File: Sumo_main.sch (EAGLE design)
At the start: 32 parts, among them U1 ATMEGA8U2AU, U2 SN65HVD3082ED, X1 MINI-USB-SCHIELD-32005-201, X2 RS485, X4 IR Sensor 1, X5 IR Sensor 2, X6 IR Sensor 3, Y1 16MHz

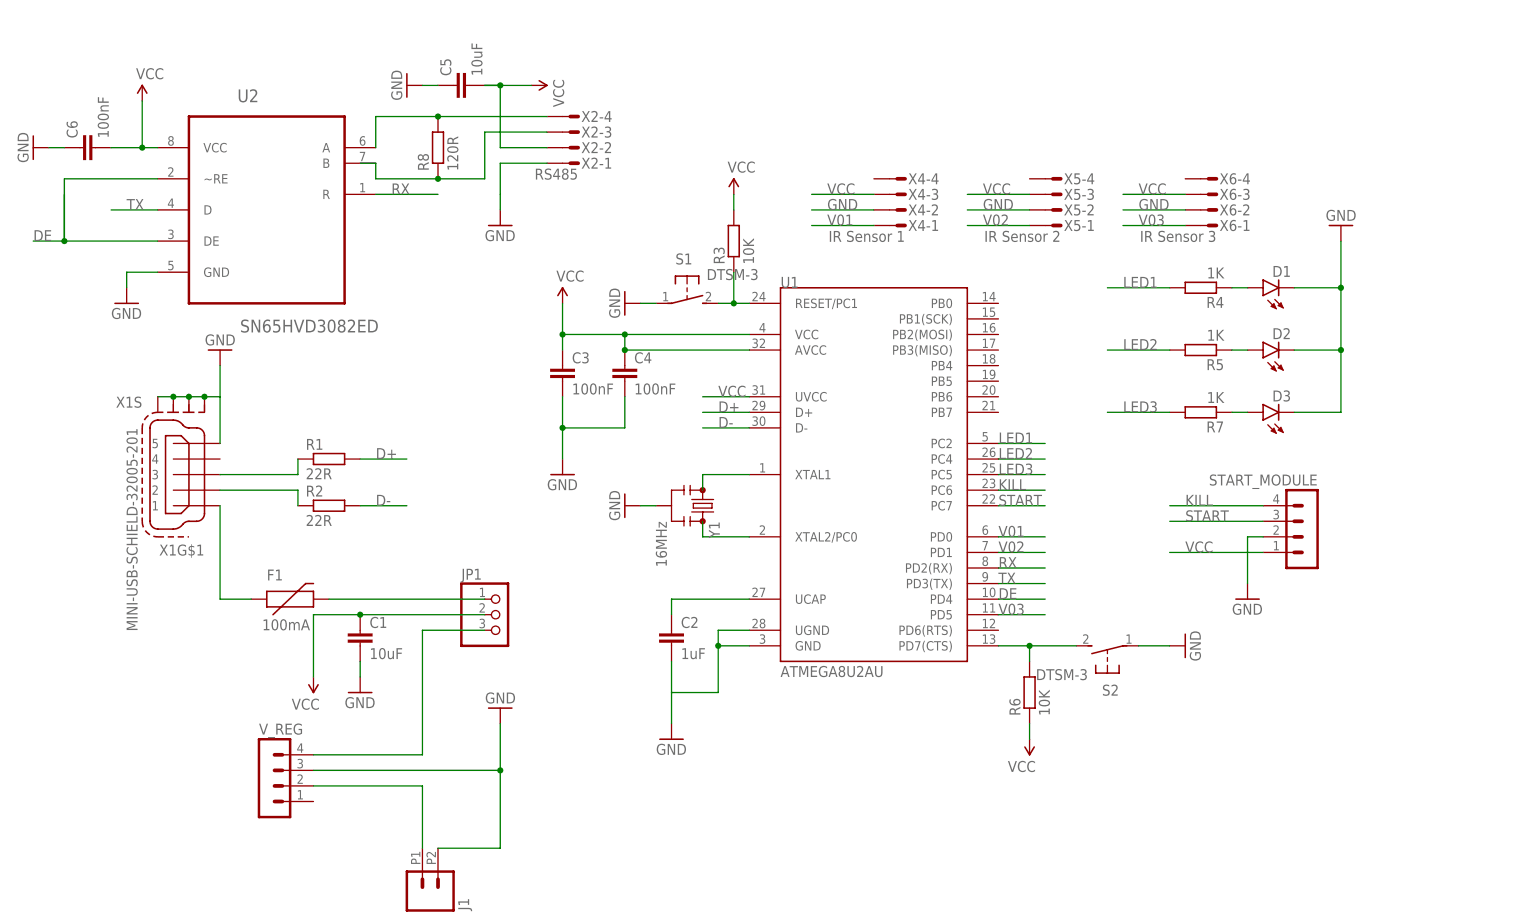
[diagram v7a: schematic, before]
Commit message: Added PNGs of schematic and board, added text to schematic and board and shortened some components' names.
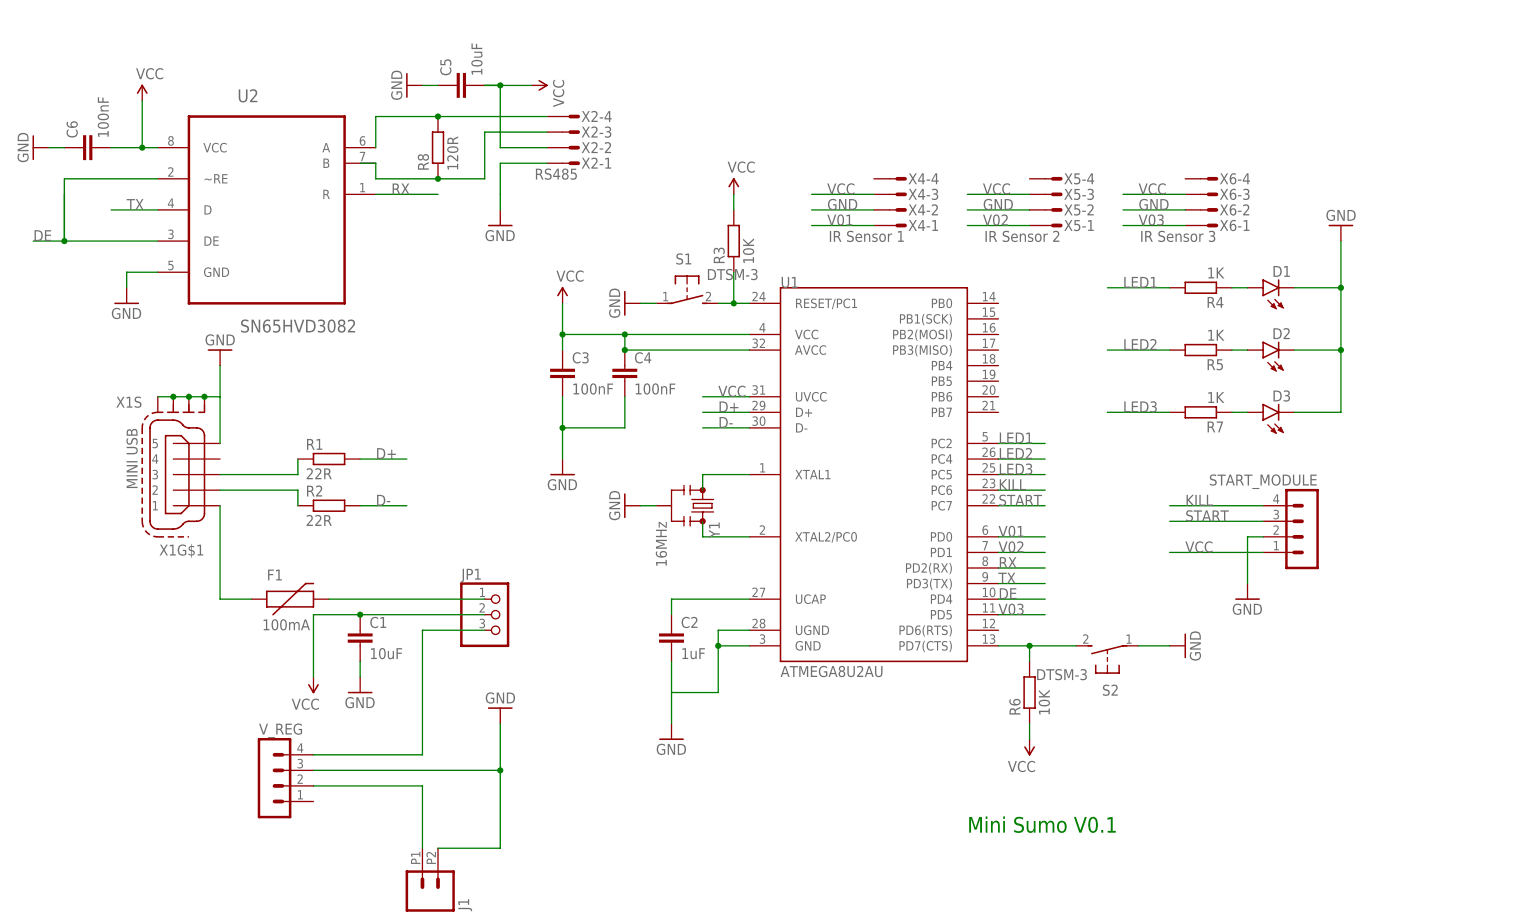
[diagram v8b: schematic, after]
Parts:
- U2: value SN65HVD3082ED -> SN65HVD3082
- X1: value MINI-USB-SCHIELD-32005-201 -> MINI USB
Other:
- note added: "Mini Sumo V0.1"
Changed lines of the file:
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@@
 <grid distance="0.1" unitdist="inch" unit="inch" style="lines" multiple="1" display="no" altdistance="0.01" altunitdist="inch" altunit="inch"/>
 <layers>
-<layer number="1" name="Top" color="4" fill="1" visible="yes" active="no"/>
-<layer number="2" name="Route2" color="1" fill="3" visible="yes" active="no"/>
-<layer number="3" name="Route3" color="4" fill="3" visible="yes" active="no"/>
-<layer number="4" name="Route4" color="1" fill="4" visible="yes" active="no"/>
-<layer number="5" name="Route5" color="4" fill="4" visible="yes" active="no"/>
-<layer number="6" name="Route6" color="1" fill="8" visible="yes" active="no"/>
-<layer number="7" name="Route7" color="4" fill="8" visible="yes" active="no"/>
-<layer number="8" name="Route8" color="1" fill="2" visible="yes" active="no"/>
-<layer number="9" name="Route9" color="4" fill="2" visible="yes" active="no"/>
-<layer number="10" name="Route10" color="1" fill="7" visible="yes" active="no"/>
-<layer number="11" name="Route11" color="4" fill="7" visible="yes" active="no"/>
-<layer number="12" name="Route12" color="1" fill="5" visible="yes" active="no"/>
-<layer number="13" name="Route13" color="4" fill="5" visible="yes" active="no"/>
-<layer number="14" name="Route14" color="1" fill="6" visible="yes" active="no"/>
-<layer number="15" name="Route15" color="4" fill="6" visible="yes" active="no"/>
-<layer number="16" name="Bottom" color="1" fill="1" visible="yes" active="no"/>
-<layer number="17" name="Pads" color="2" fill="1" visible="yes" active="no"/>
-<layer number="18" name="Vias" color="2" fill="1" visible="yes" active="no"/>
-<layer number="19" name="Unrouted" color="6" fill="1" visible="yes" active="no"/>
-<layer number="20" name="Dimension" color="15" fill="1" visible="yes" active="no"/>
-<layer number="21" name="tPlace" color="7" fill="1" visible="yes" active="no"/>
-<layer number="22" name="bPlace" color="7" fill="1" visible="yes" active="no"/>
-<layer number="23" name="tOrigins" color="15" fill="1" visible="yes" active="no"/>
-<layer number="24" name="bOrigins" color="15" fill="1" visible="yes" active="no"/>
-<layer number="25" name="tNames" color="7" fill="1" visible="yes" active="no"/>
-<layer number="26" name="bNames" color="7" fill="1" visible="yes" active="no"/>
-<layer number="27" name="tValues" color="7" fill="1" visible="yes" active="no"/>
-<layer number="28" name="bValues" color="7" fill="1" visible="yes" active="no"/>
+<layer number="1" name="Top" color="4" fill="1" visible="no" active="no"/>
+<layer number="2" name="Route2" color="1" fill="3" visible="no" active="no"/>
+<layer number="3" name="Route3" color="4" fill="3" visible="no" active="no"/>
+<layer number="4" name="Route4" color="1" fill="4" visible="no" active="no"/>
+<layer number="5" name="Route5" color="4" fill="4" visible="no" active="no"/>
+<layer number="6" name="Route6" color="1" fill="8" visible="no" active="no"/>
+<layer number="7" name="Route7" color="4" fill="8" visible="no" active="no"/>
+<layer number="8" name="Route8" color="1" fill="2" visible="no" active="no"/>
+<layer number="9" name="Route9" color="4" fill="2" visible="no" active="no"/>
+<layer number="10" name="Route10" color="1" fill="7" visible="no" active="no"/>
+<layer number="11" name="Route11" color="4" fill="7" visible="no" active="no"/>
+<layer number="12" name="Route12" color="1" fill="5" visible="no" active="no"/>
+<layer number="13" name="Route13" color="4" fill="5" visible="no" active="no"/>
+<layer number="14" name="Route14" color="1" fill="6" visible="no" active="no"/>
+<layer number="15" name="Route15" color="4" fill="6" visible="no" active="no"/>
+<layer number="16" name="Bottom" color="1" fill="1" visible="no" active="no"/>
+<layer number="17" name="Pads" color="2" fill="1" visible="no" active="no"/>
+<layer number="18" name="Vias" color="2" fill="1" visible="no" active="no"/>
+<layer number="19" name="Unrouted" color="6" fill="1" visible="no" active="no"/>
+<layer number="20" name="Dimension" color="15" fill="1" visible="no" active="no"/>
+<layer number="21" name="tPlace" color="7" fill="1" visible="no" active="no"/>
+<layer number="22" name="bPlace" color="7" fill="1" visible="no" active="no"/>
+<layer number="23" name="tOrigins" color="15" fill="1" visible="no" active="no"/>
+<layer number="24" name="bOrigins" color="15" fill="1" visible="no" active="no"/>
+<layer number="25" name="tNames" color="7" fill="1" visible="no" active="no"/>
+<layer number="26" name="bNames" color="7" fill="1" visible="no" active="no"/>
+<layer number="27" name="tValues" color="7" fill="1" visible="no" active="no"/>
+<layer number="28" name="bValues" color="7" fill="1" visible="no" active="no"/>
 <layer number="29" name="tStop" color="7" fill="3" visible="no" active="no"/>
 <layer number="30" name="bStop" color="7" fill="6" visible="no" active="no"/>
@@
 <layer number="35" name="tGlue" color="7" fill="4" visible="no" active="no"/>
 <layer number="36" name="bGlue" color="7" fill="5" visible="no" active="no"/>
-<layer number="37" name="tTest" color="7" fill="1" visible="yes" active="no"/>
-<layer number="38" name="bTest" color="7" fill="1" visible="yes" active="no"/>
+<layer number="37" name="tTest" color="7" fill="1" visible="no" active="no"/>
+<layer number="38" name="bTest" color="7" fill="1" visible="no" active="no"/>
 <layer number="39" name="tKeepout" color="4" fill="11" visible="no" active="no"/>
 <layer number="40" name="bKeepout" color="1" fill="11" visible="no" active="no"/>
@@
 <layer number="44" name="Drills" color="7" fill="1" visible="no" active="no"/>
 <layer number="45" name="Holes" color="7" fill="1" visible="no" active="no"/>
-<layer number="46" name="Milling" color="3" fill="1" visible="yes" active="no"/>
-<layer number="47" name="Measures" color="7" fill="1" visible="yes" active="no"/>
-<layer number="48" name="Document" color="7" fill="1" visible="yes" active="no"/>
-<layer number="49" name="Reference" color="7" fill="1" visible="yes" active="no"/>
-<layer number="50" name="dxf" color="7" fill="1" visible="yes" active="no"/>
-<layer number="51" name="tDocu" color="7" fill="1" visible="yes" active="no"/>
-<layer number="52" name="bDocu" color="7" fill="1" visible="yes" active="no"/>
-<layer number="53" name="tGND_GNDA" color="7" fill="9" visible="yes" active="no"/>
-<layer number="54" name="bGND_GNDA" color="1" fill="9" visible="yes" active="no"/>
-<layer number="56" name="wert" color="7" fill="1" visible="yes" active="no"/>
-<layer number="57" name="tCAD" color="7" fill="1" visible="yes" active="no"/>
-<layer number="59" name="tCarbon" color="7" fill="1" visible="yes" active="no"/>
-<layer number="60" name="bCarbon" color="7" fill="1" visible="yes" active="no"/>
+<layer number="46" name="Milling" color="3" fill="1" visible="no" active="no"/>
+<layer number="47" name="Measures" color="7" fill="1" visible="no" active="no"/>
+<layer number="48" name="Document" color="7" fill="1" visible="no" active="no"/>
+<layer number="49" name="Reference" color="7" fill="1" visible="no" active="no"/>
+<layer number="50" name="dxf" color="7" fill="1" visible="no" active="no"/>
+<layer number="51" name="tDocu" color="7" fill="1" visible="no" active="no"/>
+<layer number="52" name="bDocu" color="7" fill="1" visible="no" active="no"/>
+<layer number="53" name="tGND_GNDA" color="7" fill="9" visible="no" active="no"/>
+<layer number="54" name="bGND_GNDA" color="1" fill="9" visible="no" active="no"/>
+<layer number="56" name="wert" color="7" fill="1" visible="no" active="no"/>
+<layer number="57" name="tCAD" color="7" fill="1" visible="no" active="no"/>
+<layer number="59" name="tCarbon" color="7" fill="1" visible="no" active="no"/>
+<layer number="60" name="bCarbon" color="7" fill="1" visible="no" active="no"/>
 <layer number="90" name="Modules" color="5" fill="1" visible="yes" active="yes"/>
 <layer number="91" name="Nets" color="2" fill="1" visible="yes" active="yes"/>
@@
 <part name="GND3" library="SparkFun-Aesthetics" deviceset="GND" device=""/>
 <part name="GND4" library="SparkFun-Aesthetics" deviceset="GND" device=""/>
-<part name="X1" library="con-cypressindustries" deviceset="MINI-USB-SCHIELD-" device="32005-201"/>
+<part name="X1" library="con-cypressindustries" deviceset="MINI-USB-SCHIELD-" device="32005-201" value="MINI USB"/>
 <part name="Y1" library="SparkFun-FreqCtrl" deviceset="RESONATOR" device="4MHZ" value="16MHz"/>
 <part name="SUPPLY2" library="SparkFun-Aesthetics" deviceset="VCC" device=""/>
@@
 <part name="V_REG" library="con-lstb" deviceset="MA04-1" device=""/>
 <part name="GND11" library="SparkFun-Aesthetics" deviceset="GND" device=""/>
-<part name="U2" library="SN65HVD3082ED" deviceset="SN65HVD3082ED" device=""/>
+<part name="U2" library="SN65HVD3082ED" deviceset="SN65HVD3082ED" device="" value="SN65HVD3082"/>
 <part name="GND12" library="SparkFun-Aesthetics" deviceset="GND" device=""/>
 <part name="JP1" library="pinhead" deviceset="PINHD-1X3" device=""/>
@@
 <sheet>
 <plain>
+<text x="88.9" y="0" size="2.54" layer="91">Mini Sumo V0.1</text>
 </plain>
 <instances>
